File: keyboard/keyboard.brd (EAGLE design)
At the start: 113 x 131.5 mm, 32 parts, among them SW1 CHERRY_MX, SW10 CHERRY_MX, SW11 CHERRY_MX, SW12 CHERRY_MX, SW13 CHERRY_MX, SW14 CHERRY_MX, SW15 CHERRY_MX, SW16 CHERRY_MX, SW17 CHERRY_MX, SW18 CHERRY_MX, SW19 CHERRY_MX, SW2 CHERRY_MX, SW20 CHERRY_MX, SW21 CHERRY_MX, SW22 CHERRY_MX, SW23 CHERRY_MX, SW24 CHERRY_MX, SW25 CHERRY_MX, SW26 CHERRY_MX, SW27 CHERRY_MX, SW28 CHERRY_MX, SW3 CHERRY_MX, SW4 CHERRY_MX, SW5 CHERRY_MX, SW6 CHERRY_MX, SW7 CHERRY_MX, SW8 CHERRY_MX, SW9 CHERRY_MX

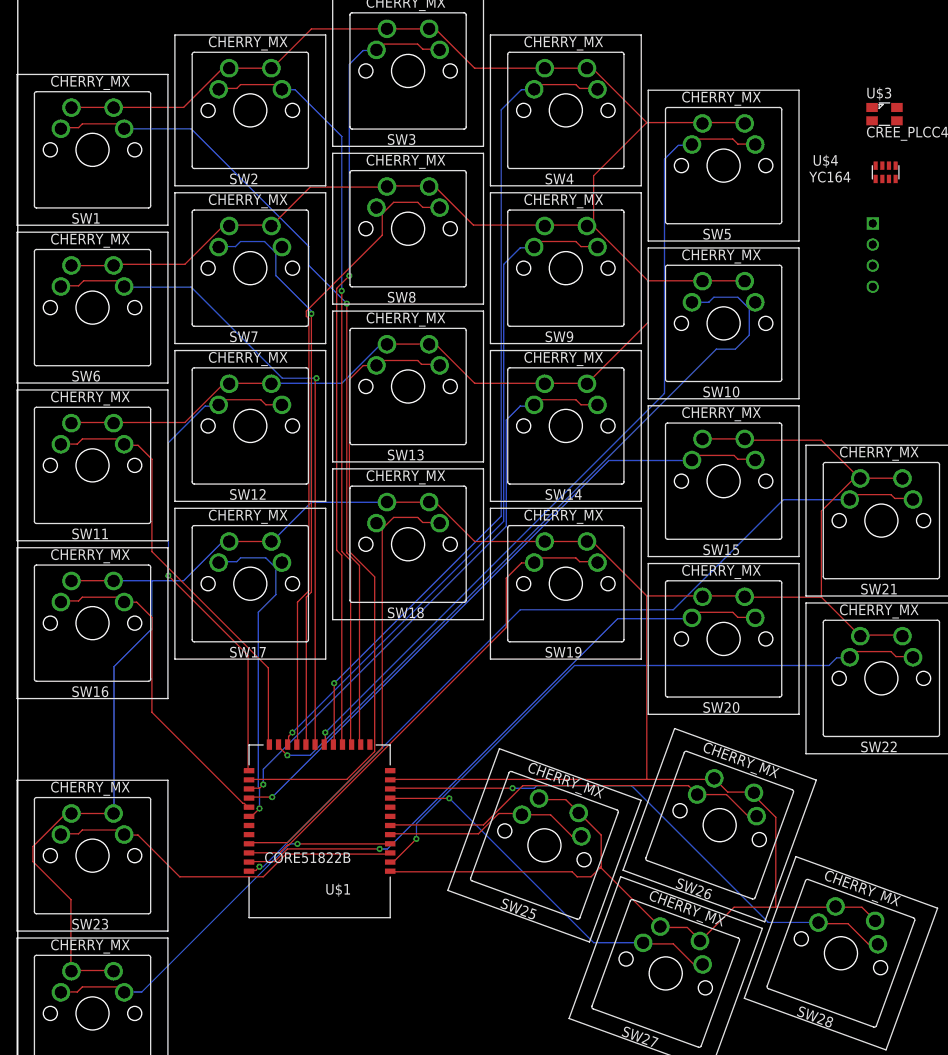
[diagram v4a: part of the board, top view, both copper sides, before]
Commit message: rearrange pins to eliminate vias
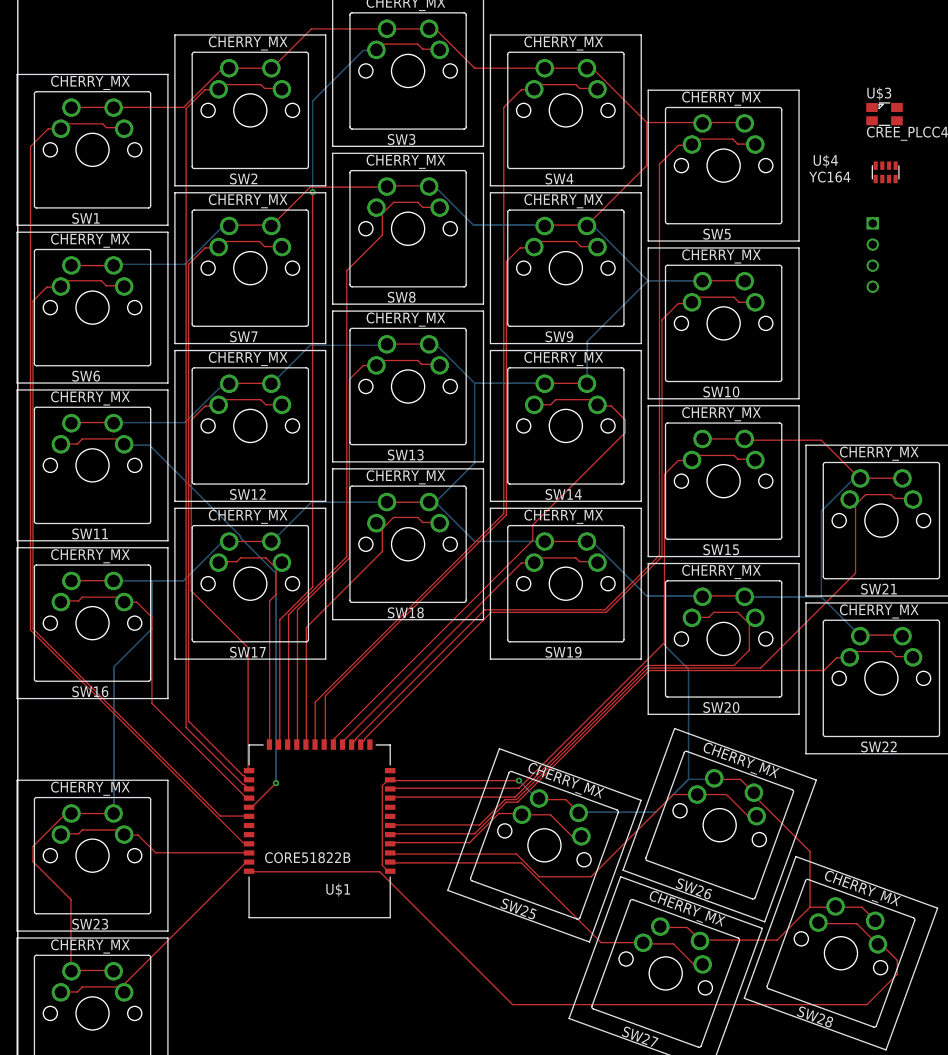
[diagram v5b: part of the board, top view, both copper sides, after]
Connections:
- net SW1: now also U$1.P17; no longer U$1.P00
- net SW10: now also U$1.P00; no longer U$1.P09
- net SW11: now also U$1.P15; no longer U$1.P10
- net SW13: now also U$1.P07; no longer U$1.P12
- net SW14: now also U$1.P03; no longer U$1.P13
- net SW15: now also U$1.P29; no longer U$1.P14
- net SW16: now also U$1.P14; no longer U$1.P15
- net SW17: now also U$1.P10; no longer U$1.P16
- net SW18: now also U$1.P06; no longer U$1.P17
- net SW19: now also U$1.P02; no longer U$1.P18
- net SW2: now also U$1.P13; no longer U$1.P01
- net SW20: now also U$1.P28; no longer U$1.P19
- net SW21: now also U$1.P25; no longer U$1.P20
- net SW22: now also U$1.P24; no longer U$1.P21
- net SW23: now also U$1.P18; no longer U$1.P22
- net SW24: now also U$1.P19; no longer U$1.P23
- net SW25: now also U$1.P23; no longer U$1.P24
- net SW26: now also U$1.P22; no longer U$1.P25
- net SW27: now also U$1.P21; no longer U$1.P28
- net SW28: now also U$1.P20; no longer U$1.P29
- net SW3: now also U$1.P09; no longer U$1.P02
- net SW4: now also U$1.P05; no longer U$1.P03
- net SW5: now also U$1.P01; no longer U$1.P04
- net SW6: now also U$1.P16; no longer U$1.P05
- net SW7: now also U$1.P12; no longer U$1.P06
- net SW8: now also U$1.P08; no longer U$1.P07
- net SW9: now also U$1.P04; no longer U$1.P08
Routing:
- net SW28: track 66.8 -> 99.4 mm, vias 1 -> 0
- net GND: track 672.0 -> 642.9 mm, vias 0 -> 1
- net SW19: track 60.4 -> 40.5 mm
- net SW23: track 43.5 -> 24.0 mm
- net SW18: track 57.0 -> 39.5 mm
- net SW24: track 47.6 -> 30.8 mm, vias 1 -> 0
- net SW13: track 74.7 -> 58.7 mm
- net SW21: track 99.0 -> 86.4 mm, vias 1 -> 0
- net SW11: track 52.5 -> 62.7 mm, vias 0 -> 1
- net SW20: track 73.7 -> 63.6 mm, vias 1 -> 0
- net SW17: track 41.2 -> 31.2 mm, vias 1 -> 0
- net SW1: track 98.9 -> 107.9 mm, vias 1 -> 0
- net SW5: track 99.7 -> 106.8 mm, vias 1 -> 0
- net SW6: track 80.1 -> 87.2 mm, vias 1 -> 0
- net SW7: track 71.0 -> 77.8 mm, vias 1 -> 0
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
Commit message: consistently align keys
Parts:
- moved SW15 1.90 mm to (85.0, 75.0)
- moved SW21 1.90 mm to (104.0, 70.2)
- moved SW20 1.90 mm to (85.0, 56.0)
- moved SW22 1.90 mm to (104.0, 51.2)
- moved SW10 1.90 mm to (85.0, 94.0)
- moved SW5 1.90 mm to (85.0, 113.0)
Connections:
- net GND: now also U$5.GND
- net SWCLK: now also U$5.SWCLK
- net SWDIO: now also U$5.SWDIO
- net VCC: now also U$5.VCC
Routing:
- net GND: track 642.9 -> 0.00 mm, vias 1 -> 0
- net SW1: track 107.9 -> 0.00 mm
- net SW5: track 106.8 -> 0.00 mm
- net SW28: track 99.4 -> 0.00 mm
- net SW4: track 98.9 -> 0.00 mm
- net SW2: track 98.2 -> 0.00 mm
- net SW3: track 97.7 -> 0.00 mm, vias 1 -> 0
- net SW6: track 87.2 -> 0.00 mm
- net SW10: track 86.9 -> 0.00 mm
- net SW21: track 86.4 -> 0.00 mm
- net SW9: track 79.6 -> 0.00 mm
- net SW8: track 78.4 -> 0.00 mm
- net SW7: track 77.8 -> 0.00 mm
- net SW15: track 72.7 -> 0.00 mm
- net SW22: track 72.4 -> 0.00 mm
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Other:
- outline, holes or cut-outs redrawn

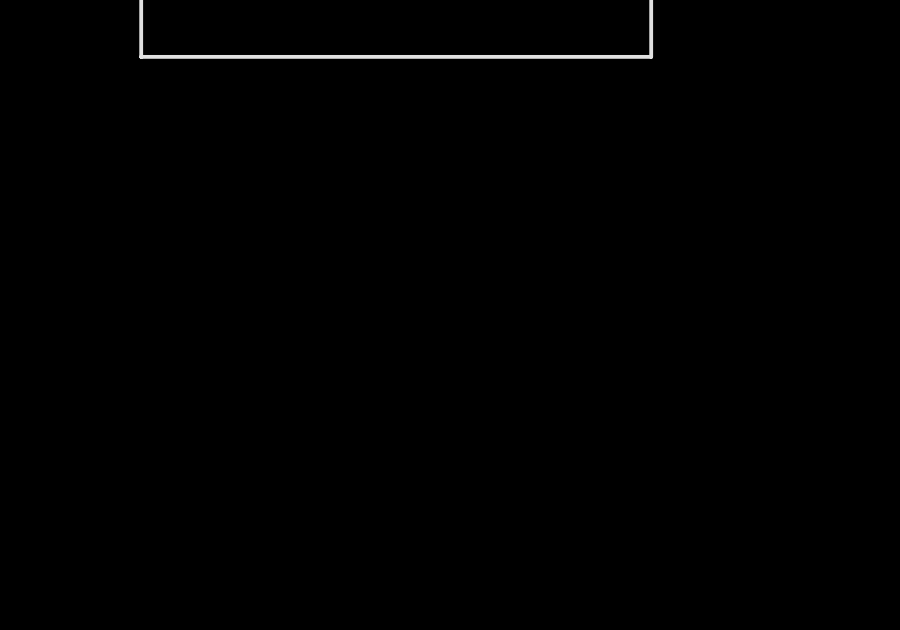
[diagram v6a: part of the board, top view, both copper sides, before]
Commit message: add MCP73831T LiPo CMC
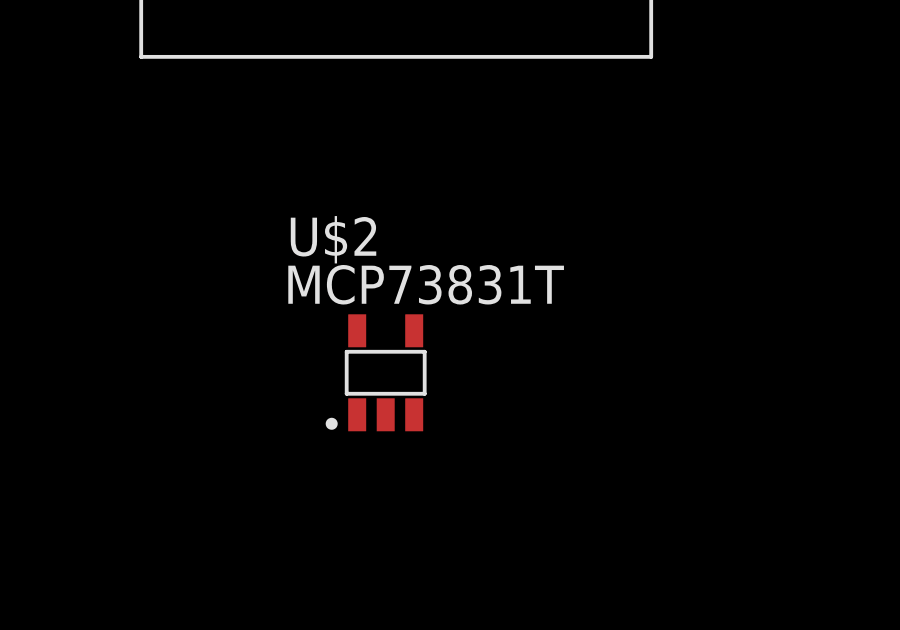
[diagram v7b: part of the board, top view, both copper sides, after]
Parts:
- added U$2: MCP73831T, mcp73831t:MCP73831T
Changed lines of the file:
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@@
 <layers>
 <layer number="1" name="Top" color="4" fill="1" visible="yes" active="yes"/>
+<layer number="2" name="Route2" color="1" fill="3" visible="no" active="yes"/>
+<layer number="15" name="Route15" color="4" fill="6" visible="no" active="yes"/>
 <layer number="16" name="Bottom" color="1" fill="1" visible="yes" active="yes"/>
 <layer number="17" name="Pads" color="2" fill="1" visible="yes" active="yes"/>
@@
 <element name="SW27" library="cherry_mx" package="CHERRY_MX" value="CHERRY_MX" x="78.0267" y="13.81679375" rot="R340"/>
 <element name="SW28" library="cherry_mx" package="CHERRY_MX" value="CHERRY_MX" x="99.130053125" y="16.245490625" rot="R340"/>
+<element name="U$2" library="mcp73831t" package="MCP73831T" value="MCP73831T" x="36" y="10"/>
 </elements>
 <signals>
